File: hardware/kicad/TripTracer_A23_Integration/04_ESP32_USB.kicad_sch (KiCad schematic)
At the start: 13 parts, among them J201 GCT USB4105-GF-A, U201 ESP32-S3-MINI-1-N8

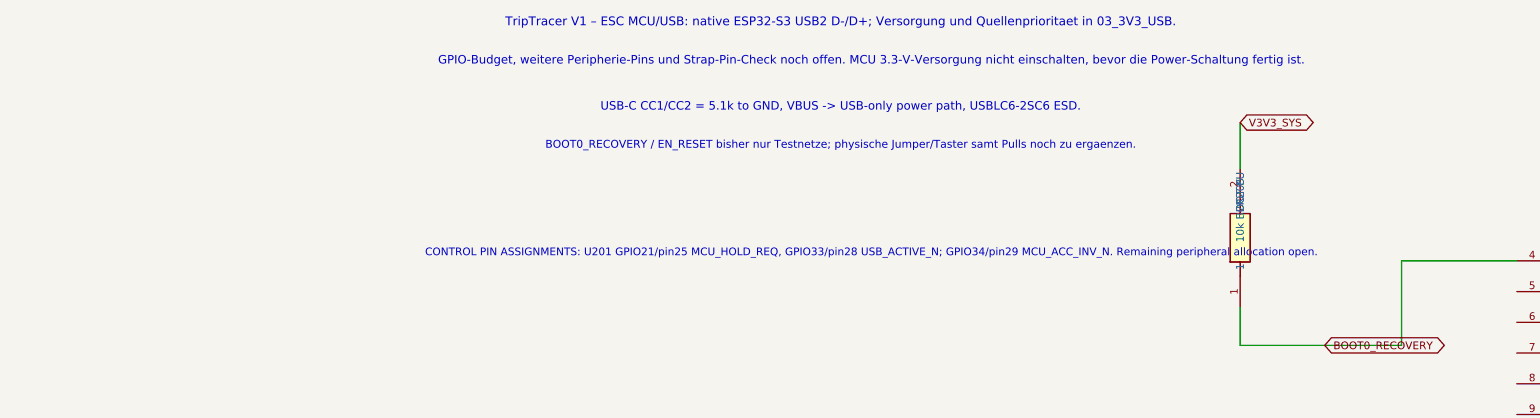
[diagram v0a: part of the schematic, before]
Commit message: TripPower A23 integrated LAB: annotate 33 genuinely unused host ESP32 GPIOs NC and link missing TripPower_Sym library; no electrical power change
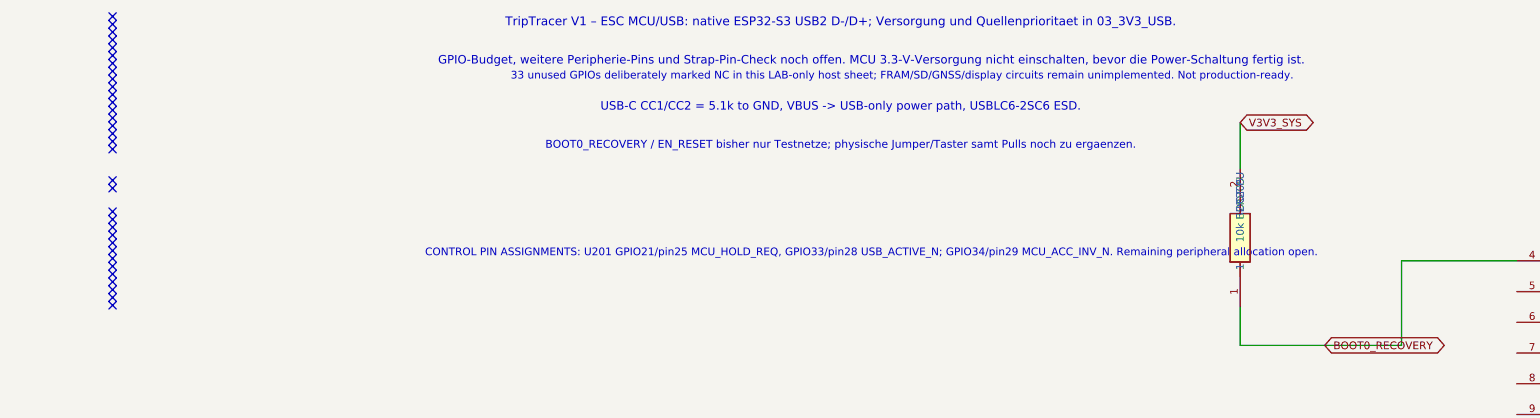
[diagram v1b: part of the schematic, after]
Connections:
- no-connect marks 2 -> 35
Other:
- note added: "33 unused GPIOs deliberately marked NC in this LAB-only host sheet; FRAM/SD/GNSS/display circuits remain unimplemented. Not production-ready."
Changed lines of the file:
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@@
 (wire (pts (xy 300.99 177.8) (xy 311.15 177.8)) (stroke (width 0) (type default)))
 (wire (pts (xy 300.99 182.88) (xy 311.15 182.88)) (stroke (width 0) (type default)))
+(text "33 unused GPIOs deliberately marked NC in this LAB-only host sheet; FRAM/SD/GNSS/display circuits remain unimplemented. Not production-ready." (at 209.55 25.4 0) (effects (font (size 1.27 1.27))))
+(no_connect (at 79.03 15.48))
+(no_connect (at 79.03 16.77))
+(no_connect (at 79.03 18.06))
+(no_connect (at 79.03 19.35))
+(no_connect (at 79.03 20.65))
+(no_connect (at 79.03 21.94))
+(no_connect (at 79.03 23.23))
+(no_connect (at 79.03 24.52))
+(no_connect (at 79.03 25.81))
+(no_connect (at 79.03 27.10))
+(no_connect (at 79.03 28.39))
+(no_connect (at 79.03 29.68))
+(no_connect (at 79.03 30.97))
+(no_connect (at 79.03 32.26))
+(no_connect (at 79.03 33.55))
+(no_connect (at 79.03 34.84))
+(no_connect (at 79.03 36.13))
+(no_connect (at 79.03 37.42))
+(no_connect (at 79.03 42.58))
+(no_connect (at 79.03 43.87))
+(no_connect (at 79.03 47.74))
+(no_connect (at 79.03 49.03))
+(no_connect (at 79.03 50.32))
+(no_connect (at 79.03 51.61))
+(no_connect (at 79.03 52.90))
+(no_connect (at 79.03 54.19))
+(no_connect (at 79.03 55.48))
+(no_connect (at 79.03 56.77))
+(no_connect (at 79.03 58.06))
+(no_connect (at 79.03 59.35))
+(no_connect (at 79.03 60.65))
+(no_connect (at 79.03 61.94))
+(no_connect (at 79.03 63.23))
 )
